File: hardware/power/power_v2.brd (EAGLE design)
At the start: 92 x 92 mm, 61 parts, among them J1 FASTON1289_ST, J2 FASTON1289_ST, J3 12v, J4 5v, J5 XT30PW-F, J6 XT30PW-F, J7 XT30PW-F, J8 XT30PW-F, Q1 MMBT5401L, Q2 PSMN1R0-40YSH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

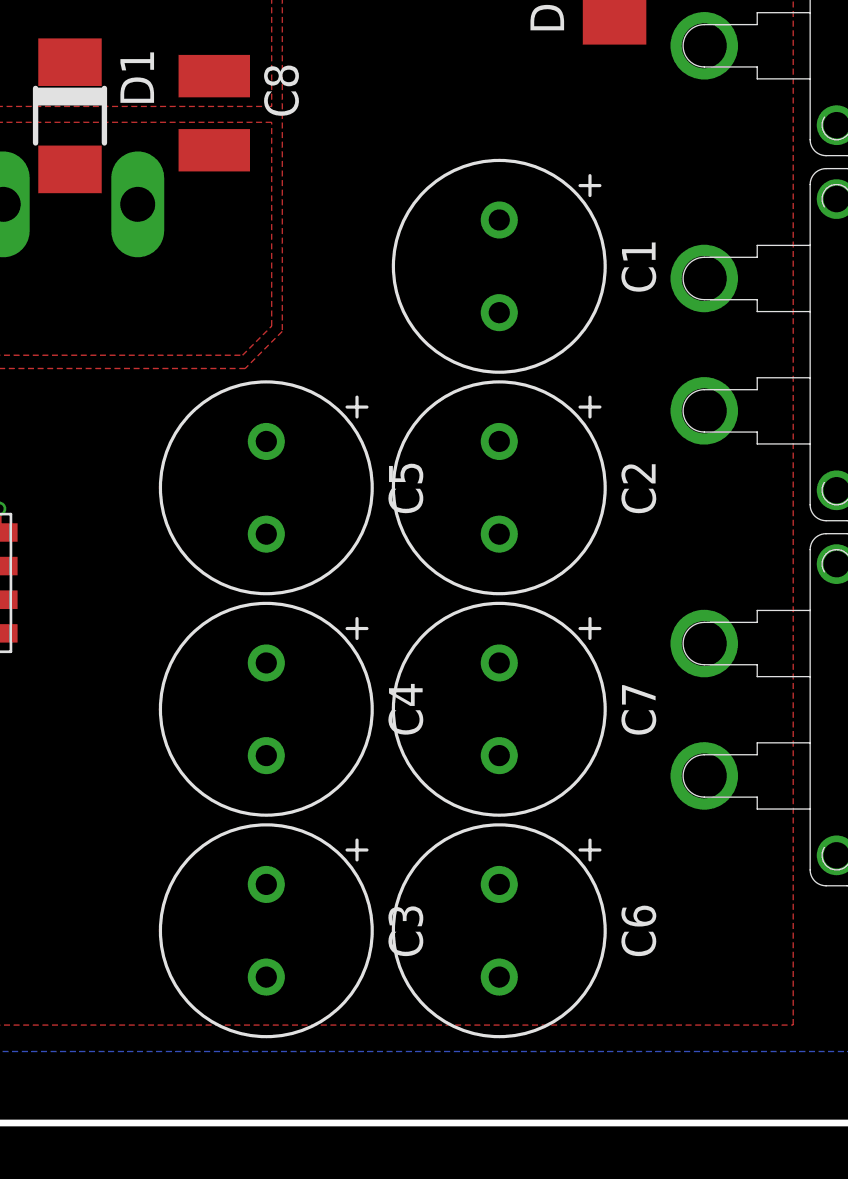
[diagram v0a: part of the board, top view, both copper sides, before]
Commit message: Moved caps a bit more
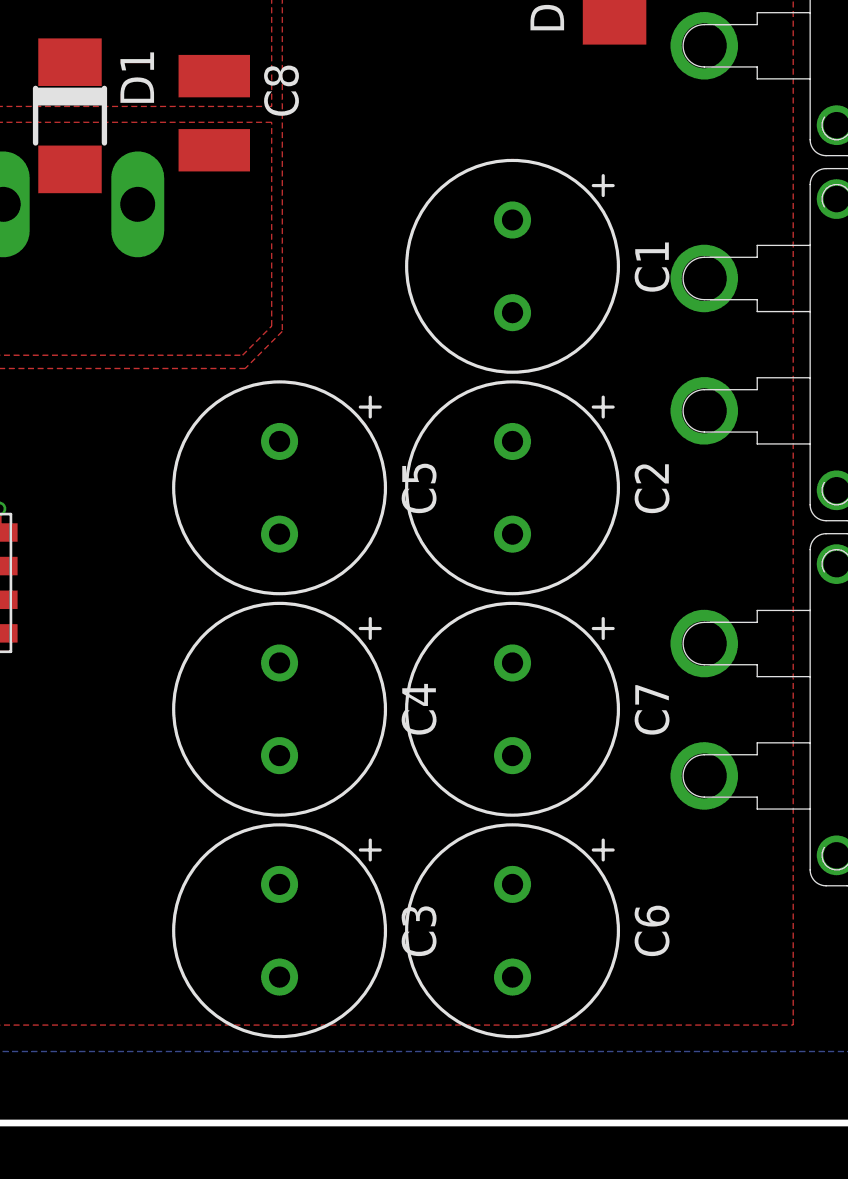
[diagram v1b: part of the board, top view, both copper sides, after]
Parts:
- moved C1 0.50 mm to (69.7, 32.4)
- moved C2 0.50 mm to (69.7, 24.0)
- moved C3 0.50 mm to (60.9, 7.26)
- moved C4 0.50 mm to (60.9, 15.6)
- moved C5 0.50 mm to (60.9, 24.0)
- moved C6 0.50 mm to (69.7, 7.26)
- moved C7 0.50 mm to (69.7, 15.6)
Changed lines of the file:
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@@
 </layers>
 <board>
-<fusionsync huburn="a.YnVzaW5lc3M6Z21haWwyMjE5MTc" projecturn="a.YnVzaW5lc3M6Z21haWwyMjE5MTcjMjAxOTA2MjkyMDE0MTU5NzY" f3durn="urn:adsk.wipprod:dm.lineage:MB3VqYkNRX6Sa_ecpPTqbA" pcbguid="9dcfff74-9686-4bdf-a14e-dd144a326308" lastpulledtime="2020-01-18T04:37:27Z" lastsyncedchangeguid="30fce54c-48fa-602d-77f9-6023b09cda53"/>
+<fusionsync huburn="a.YnVzaW5lc3M6Z21haWwyMjE5MTc" projecturn="a.YnVzaW5lc3M6Z21haWwyMjE5MTcjMjAxOTA2MjkyMDE0MTU5NzY" f3durn="urn:adsk.wipprod:dm.lineage:MB3VqYkNRX6Sa_ecpPTqbA" pcbguid="9dcfff74-9686-4bdf-a14e-dd144a326308" lastpulledtime="2020-01-18T04:37:27Z" lastsyncedchangeguid="f8bd3ab9-24a6-9b98-5fd5-58b79cb29ea8"/>
 <plain>
 <hole x="39" y="89" drill="3.4"/>
@@
 <attribute name="VALUE" x="18.615" y="81.885" size="1.27" layer="27" rot="R90"/>
 </element>
-<element name="C1" library="timlib" library_urn="urn:adsk.eagle:library:16152524" package="C_ELEC_8X11_5" package3d_urn="urn:adsk.eagle:package:16381562/2" value="220uf" x="69.1975" y="32.359159375" smashed="yes" rot="R270">
-<attribute name="NAME" x="73.8325" y="32.359159375" size="1.27" layer="25" rot="R270" align="bottom-center"/>
-<attribute name="VALUE" x="64.5625" y="32.359159375" size="1.27" layer="27" rot="R270" align="top-center"/>
-</element>
-<element name="C2" library="timlib" library_urn="urn:adsk.eagle:library:16152524" package="C_ELEC_8X11_5" package3d_urn="urn:adsk.eagle:package:16381562/2" value="220uf" x="69.1975" y="23.993328125" smashed="yes" rot="R270">
-<attribute name="NAME" x="73.8325" y="23.993328125" size="1.27" layer="25" rot="R270" align="bottom-center"/>
-<attribute name="VALUE" x="64.5625" y="23.993328125" size="1.27" layer="27" rot="R270" align="top-center"/>
-</element>
-<element name="C3" library="timlib" library_urn="urn:adsk.eagle:library:16152524" package="C_ELEC_8X11_5" package3d_urn="urn:adsk.eagle:package:16381562/2" value="220uf" x="60.3975" y="7.261665625" smashed="yes" rot="R270">
-<attribute name="NAME" x="65.0325" y="7.261665625" size="1.27" layer="25" rot="R270" align="bottom-center"/>
-<attribute name="VALUE" x="55.7625" y="7.261665625" size="1.27" layer="27" rot="R270" align="top-center"/>
-</element>
-<element name="C4" library="timlib" library_urn="urn:adsk.eagle:library:16152524" package="C_ELEC_8X11_5" package3d_urn="urn:adsk.eagle:package:16381562/2" value="220uf" x="60.3975" y="15.627496875" smashed="yes" rot="R270">
-<attribute name="NAME" x="65.0325" y="15.627496875" size="1.27" layer="25" rot="R270" align="bottom-center"/>
-<attribute name="VALUE" x="55.7625" y="15.627496875" size="1.27" layer="27" rot="R270" align="top-center"/>
-</element>
-<element name="C5" library="timlib" library_urn="urn:adsk.eagle:library:16152524" package="C_ELEC_8X11_5" package3d_urn="urn:adsk.eagle:package:16381562/2" value="220uf" x="60.3975" y="23.993328125" smashed="yes" rot="R270">
-<attribute name="NAME" x="65.0325" y="23.993328125" size="1.27" layer="25" rot="R270" align="bottom-center"/>
-<attribute name="VALUE" x="55.7625" y="23.993328125" size="1.27" layer="27" rot="R270" align="top-center"/>
-</element>
-<element name="C6" library="timlib" library_urn="urn:adsk.eagle:library:16152524" package="C_ELEC_8X11_5" package3d_urn="urn:adsk.eagle:package:16381562/2" value="220uf" x="69.1975" y="7.261665625" smashed="yes" rot="R270">
-<attribute name="NAME" x="73.8325" y="7.261665625" size="1.27" layer="25" rot="R270" align="bottom-center"/>
-<attribute name="VALUE" x="64.5625" y="7.261665625" size="1.27" layer="27" rot="R270" align="top-center"/>
-</element>
-<element name="C7" library="timlib" library_urn="urn:adsk.eagle:library:16152524" package="C_ELEC_8X11_5" package3d_urn="urn:adsk.eagle:package:16381562/2" value="220uf" x="69.1975" y="15.627496875" smashed="yes" rot="R270">
-<attribute name="NAME" x="73.8325" y="15.627496875" size="1.27" layer="25" rot="R270" align="bottom-center"/>
-<attribute name="VALUE" x="64.5625" y="15.627496875" size="1.27" layer="27" rot="R270" align="top-center"/>
+<element name="C1" library="timlib" library_urn="urn:adsk.eagle:library:16152524" package="C_ELEC_8X11_5" package3d_urn="urn:adsk.eagle:package:16381562/2" value="220uf" x="69.6975" y="32.359159375" smashed="yes" rot="R270">
+<attribute name="NAME" x="74.3325" y="32.359159375" size="1.27" layer="25" rot="R270" align="bottom-center"/>
+<attribute name="VALUE" x="65.0625" y="32.359159375" size="1.27" layer="27" rot="R270" align="top-center"/>
+</element>
+<element name="C2" library="timlib" library_urn="urn:adsk.eagle:library:16152524" package="C_ELEC_8X11_5" package3d_urn="urn:adsk.eagle:package:16381562/2" value="220uf" x="69.6975" y="23.993328125" smashed="yes" rot="R270">
+<attribute name="NAME" x="74.3325" y="23.993328125" size="1.27" layer="25" rot="R270" align="bottom-center"/>
+<attribute name="VALUE" x="65.0625" y="23.993328125" size="1.27" layer="27" rot="R270" align="top-center"/>
+</element>
+<element name="C3" library="timlib" library_urn="urn:adsk.eagle:library:16152524" package="C_ELEC_8X11_5" package3d_urn="urn:adsk.eagle:package:16381562/2" value="220uf" x="60.8975" y="7.261665625" smashed="yes" rot="R270">
+<attribute name="NAME" x="65.5325" y="7.261665625" size="1.27" layer="25" rot="R270" align="bottom-center"/>
+<attribute name="VALUE" x="56.2625" y="7.261665625" size="1.27" layer="27" rot="R270" align="top-center"/>
+</element>
+<element name="C4" library="timlib" library_urn="urn:adsk.eagle:library:16152524" package="C_ELEC_8X11_5" package3d_urn="urn:adsk.eagle:package:16381562/2" value="220uf" x="60.8975" y="15.627496875" smashed="yes" rot="R270">
+<attribute name="NAME" x="65.5325" y="15.627496875" size="1.27" layer="25" rot="R270" align="bottom-center"/>
+<attribute name="VALUE" x="56.2625" y="15.627496875" size="1.27" layer="27" rot="R270" align="top-center"/>
+</element>
+<element name="C5" library="timlib" library_urn="urn:adsk.eagle:library:16152524" package="C_ELEC_8X11_5" package3d_urn="urn:adsk.eagle:package:16381562/2" value="220uf" x="60.8975" y="23.993328125" smashed="yes" rot="R270">
+<attribute name="NAME" x="65.5325" y="23.993328125" size="1.27" layer="25" rot="R270" align="bottom-center"/>
+<attribute name="VALUE" x="56.2625" y="23.993328125" size="1.27" layer="27" rot="R270" align="top-center"/>
+</element>
+<element name="C6" library="timlib" library_urn="urn:adsk.eagle:library:16152524" package="C_ELEC_8X11_5" package3d_urn="urn:adsk.eagle:package:16381562/2" value="220uf" x="69.6975" y="7.261665625" smashed="yes" rot="R270">
+<attribute name="NAME" x="74.3325" y="7.261665625" size="1.27" layer="25" rot="R270" align="bottom-center"/>
+<attribute name="VALUE" x="65.0625" y="7.261665625" size="1.27" layer="27" rot="R270" align="top-center"/>
+</element>
+<element name="C7" library="timlib" library_urn="urn:adsk.eagle:library:16152524" package="C_ELEC_8X11_5" package3d_urn="urn:adsk.eagle:package:16381562/2" value="220uf" x="69.6975" y="15.627496875" smashed="yes" rot="R270">
+<attribute name="NAME" x="74.3325" y="15.627496875" size="1.27" layer="25" rot="R270" align="bottom-center"/>
+<attribute name="VALUE" x="65.0625" y="15.627496875" size="1.27" layer="27" rot="R270" align="top-center"/>
 </element>
 <element name="U$1" library="timlib" library_urn="urn:adsk.eagle:library:16152524" package="VSSOP_DGS_10" package3d_urn="urn:adsk.eagle:package:16499421/2" value="LM5069_DGS_10" x="19.1" y="32.19" smashed="yes" rot="R270"/>

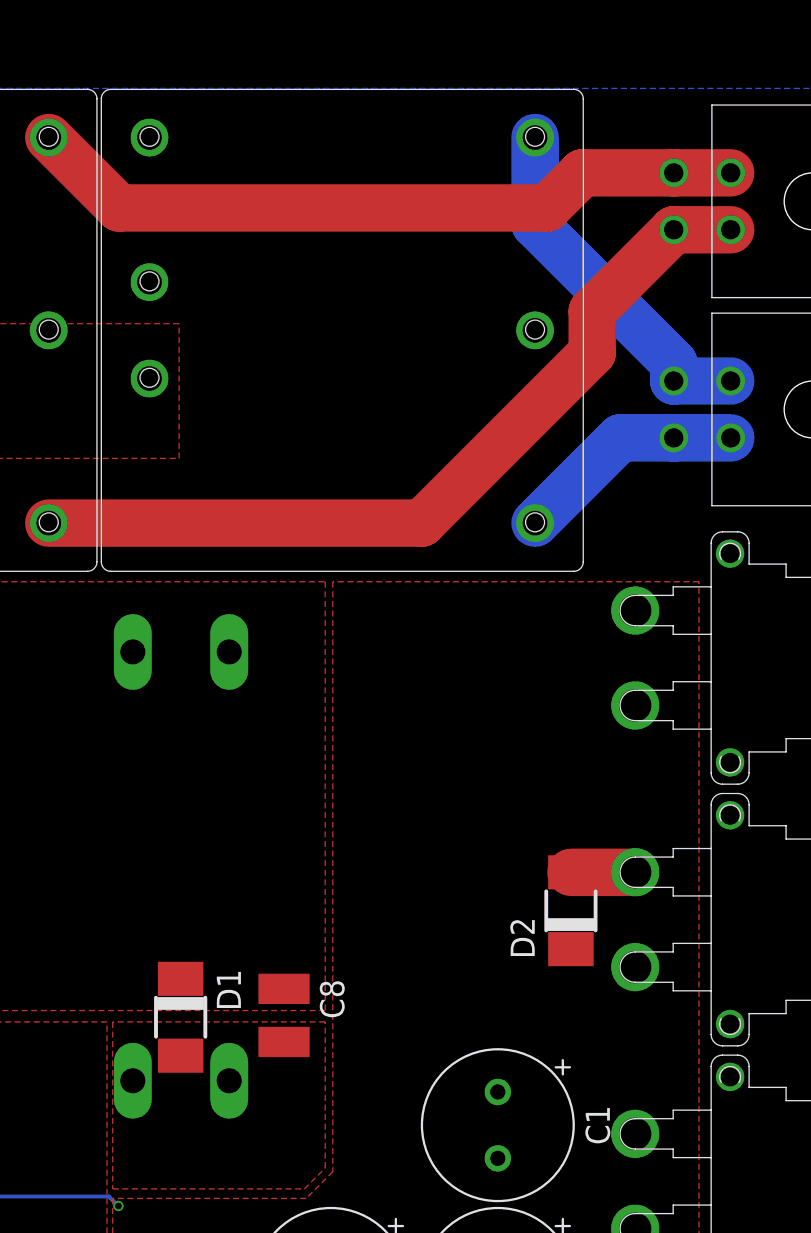
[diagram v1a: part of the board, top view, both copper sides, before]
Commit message: Aligned blades better
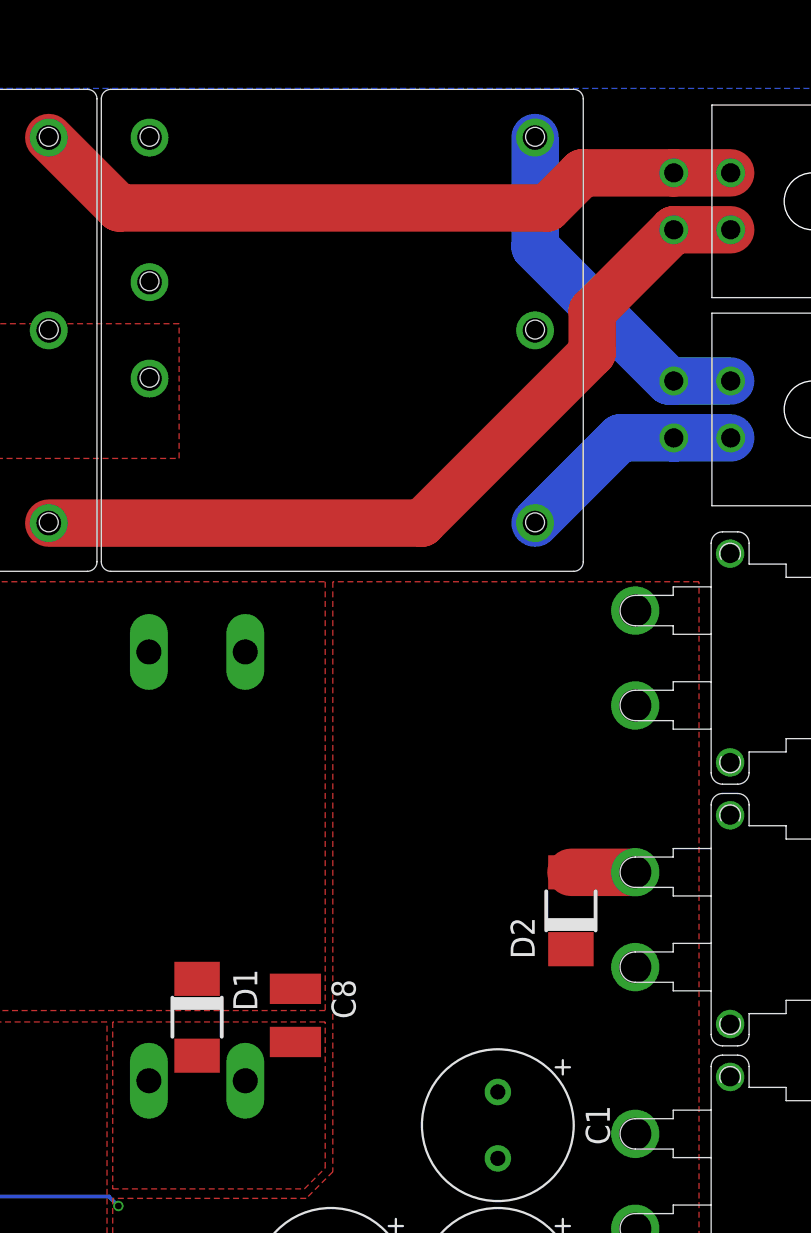
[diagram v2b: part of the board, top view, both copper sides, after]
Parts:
- moved D1 0.86 mm to (53.8, 38.0)
- moved J1 0.85 mm to (53.8, 57.3)
- moved J2 0.85 mm to (53.8, 34.7)
- moved C8 0.60 mm to (59.0, 38.1)
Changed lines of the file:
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@@
 </layers>
 <board>
-<fusionsync huburn="a.YnVzaW5lc3M6Z21haWwyMjE5MTc" projecturn="a.YnVzaW5lc3M6Z21haWwyMjE5MTcjMjAxOTA2MjkyMDE0MTU5NzY" f3durn="urn:adsk.wipprod:dm.lineage:MB3VqYkNRX6Sa_ecpPTqbA" pcbguid="9dcfff74-9686-4bdf-a14e-dd144a326308" lastpulledtime="2020-01-18T04:37:27Z" lastsyncedchangeguid="f8bd3ab9-24a6-9b98-5fd5-58b79cb29ea8"/>
+<fusionsync huburn="a.YnVzaW5lc3M6Z21haWwyMjE5MTc" projecturn="a.YnVzaW5lc3M6Z21haWwyMjE5MTcjMjAxOTA2MjkyMDE0MTU5NzY" f3durn="urn:adsk.wipprod:dm.lineage:MB3VqYkNRX6Sa_ecpPTqbA" pcbguid="9dcfff74-9686-4bdf-a14e-dd144a326308" lastpulledtime="2020-01-18T04:37:27Z" lastsyncedchangeguid="949c5408-da32-ad4a-ba52-90464d57dd80"/>
 <plain>
 <hole x="39" y="89" drill="3.4"/>
@@
 <element name="J7" library="timlib" library_urn="urn:adsk.eagle:library:16152524" package="XT30PW-F" package3d_urn="urn:adsk.eagle:package:16203166/7" value="XT30PW-F" x="81.94" y="29.4" smashed="yes" rot="R270"/>
 <element name="J8" library="timlib" library_urn="urn:adsk.eagle:library:16152524" package="XT30PW-F" package3d_urn="urn:adsk.eagle:package:16203166/7" value="XT30PW-F" x="81.94" y="15.61" smashed="yes" rot="R270"/>
-<element name="J1" library="timlib" library_urn="urn:adsk.eagle:library:16152524" package="FASTON_1289-ST" package3d_urn="urn:adsk.eagle:package:16406409/3" value="FASTON1289_ST" x="53" y="57.3" locked="yes" smashed="yes" rot="MR180"/>
-<element name="J2" library="timlib" library_urn="urn:adsk.eagle:library:16152524" package="FASTON_1289-ST" package3d_urn="urn:adsk.eagle:package:16406409/3" value="FASTON1289_ST" x="53" y="34.7" locked="yes" smashed="yes" rot="MR0"/>
+<element name="J1" library="timlib" library_urn="urn:adsk.eagle:library:16152524" package="FASTON_1289-ST" package3d_urn="urn:adsk.eagle:package:16406409/3" value="FASTON1289_ST" x="53.847" y="57.3" locked="yes" smashed="yes" rot="MR180"/>
+<element name="J2" library="timlib" library_urn="urn:adsk.eagle:library:16152524" package="FASTON_1289-ST" package3d_urn="urn:adsk.eagle:package:16406409/3" value="FASTON1289_ST" x="53.847" y="34.7" locked="yes" smashed="yes" rot="MR0"/>
 <element name="J3" library="timlib" library_urn="urn:adsk.eagle:library:16152524" package="MOLEX_4_RA" package3d_urn="urn:adsk.eagle:package:16152611/3" value="12v" x="86.29" y="81.05" smashed="yes" rot="R90"/>
 <element name="J4" library="timlib" library_urn="urn:adsk.eagle:library:16152524" package="MOLEX_4_RA" package3d_urn="urn:adsk.eagle:package:16152611/3" value="5v" x="86.29" y="70.08" smashed="yes" rot="R90"/>
@@
 </element>
 <element name="U$1" library="timlib" library_urn="urn:adsk.eagle:library:16152524" package="VSSOP_DGS_10" package3d_urn="urn:adsk.eagle:package:16499421/2" value="LM5069_DGS_10" x="19.1" y="32.19" smashed="yes" rot="R270"/>
-<element name="D1" library="timlib" library_urn="urn:adsk.eagle:library:16152524" package="DO-214AC" package3d_urn="urn:adsk.eagle:package:16356227/6" value="SMAJ30A" x="52.98213125" y="38.045" smashed="yes" rot="R270">
-<attribute name="NAME" x="54.88713125" y="40.585" size="1.27" layer="25" rot="R270"/>
-<attribute name="VALUE" x="49.80713125" y="40.585" size="1.27" layer="27" rot="R270"/>
-</element>
-<element name="C8" library="timlib" library_urn="urn:adsk.eagle:library:16152524" package="C1210" package3d_urn="urn:adsk.eagle:package:23619/2" value="0.01uF" x="58.429996875" y="38.145" smashed="yes" rot="R270">
-<attribute name="NAME" x="60.334996875" y="40.05" size="1.27" layer="25" rot="R270"/>
-<attribute name="VALUE" x="55.254996875" y="40.05" size="1.27" layer="27" rot="R270"/>
+<element name="D1" library="timlib" library_urn="urn:adsk.eagle:library:16152524" package="DO-214AC" package3d_urn="urn:adsk.eagle:package:16356227/6" value="SMAJ30A" x="53.847" y="38.045" smashed="yes" rot="R270">
+<attribute name="NAME" x="55.752" y="40.585" size="1.27" layer="25" rot="R270"/>
+<attribute name="VALUE" x="50.672" y="40.585" size="1.27" layer="27" rot="R270"/>
+</element>
+<element name="C8" library="timlib" library_urn="urn:adsk.eagle:library:16152524" package="C1210" package3d_urn="urn:adsk.eagle:package:23619/2" value="0.01uF" x="59.029996875" y="38.145" smashed="yes" rot="R270">
+<attribute name="NAME" x="60.934996875" y="40.05" size="1.27" layer="25" rot="R270"/>
+<attribute name="VALUE" x="55.854996875" y="40.05" size="1.27" layer="27" rot="R270"/>
 </element>
 <element name="R1" library="rcl" library_urn="urn:adsk.eagle:library:334" package="R0603" package3d_urn="urn:adsk.eagle:package:23555/3" value="47.5k" x="13.61" y="29.2" smashed="yes">
@@
 <contactref element="J4" pad="CIRCUIT3"/>
 <contactref element="U1" pad="P$5"/>
-<wire x1="71.66" y1="84.41" x2="71.66" y2="79.84" width="2.5" layer="16"/>
-<wire x1="78.97" y1="72.53" x2="78.97" y2="71.58" width="2.5" layer="16"/>
-<wire x1="71.66" y1="79.84" x2="78.97" y2="72.53" width="2.5" layer="16"/>
+<wire x1="71.66" y1="84.41" x2="71.66" y2="78.64" width="2.5" layer="16"/>
+<wire x1="78.97" y1="71.58" x2="78.72" y2="71.58" width="2.5" layer="16"/>
+<wire x1="78.72" y1="71.58" x2="71.66" y2="78.64" width="2.5" layer="16"/>
 <wire x1="78.97" y1="71.58" x2="81.97" y2="71.58" width="2.5" layer="16"/>
 </signal>
